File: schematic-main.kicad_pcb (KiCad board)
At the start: 2 copper layers, 100 x 100 mm, 115 parts, among them J1 Fell_Cell_Conn_01x02_Pin, J2 CAN, J3 P_Valve, J5 PWM_Out, J7 Axilary_Out, J8 Temp, J9 Analog_In, P1 USB_C_Plug_USB2.0, U1 LM76202-Q1, U2 TPS62933, U3 USBLC6-2P6, U4 ESP32-S3FN8, U5 SN65HVD232, U6 LM5013DDAR, U7 PC817, U8 PC817, U9 PC817

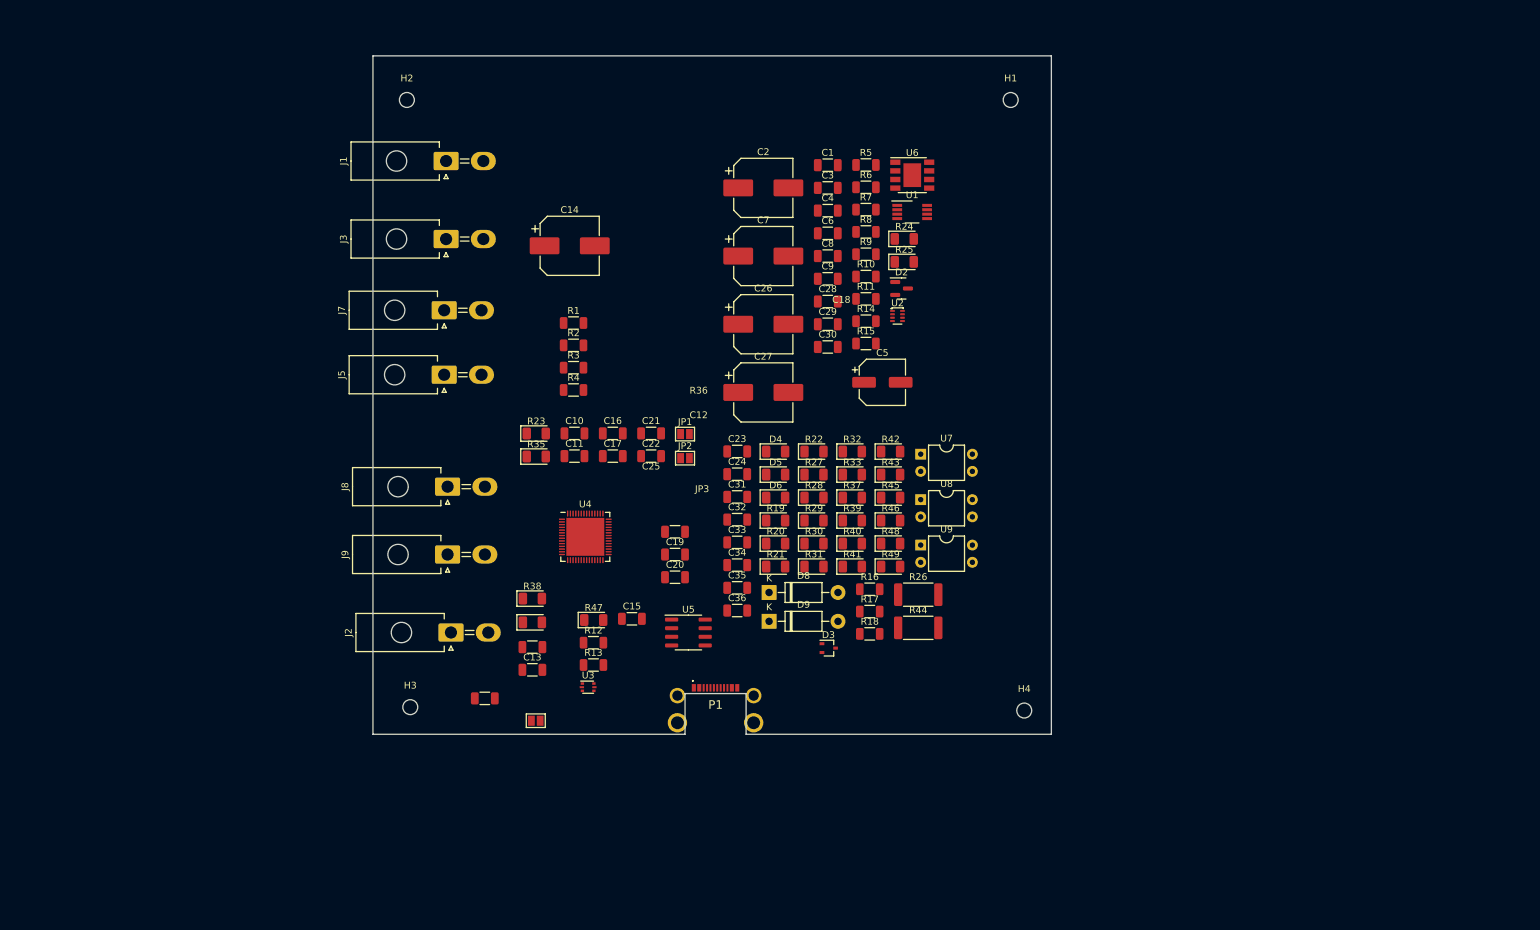
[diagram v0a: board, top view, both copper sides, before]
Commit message: Change FC connector to 10pin & ideal diode sircuit
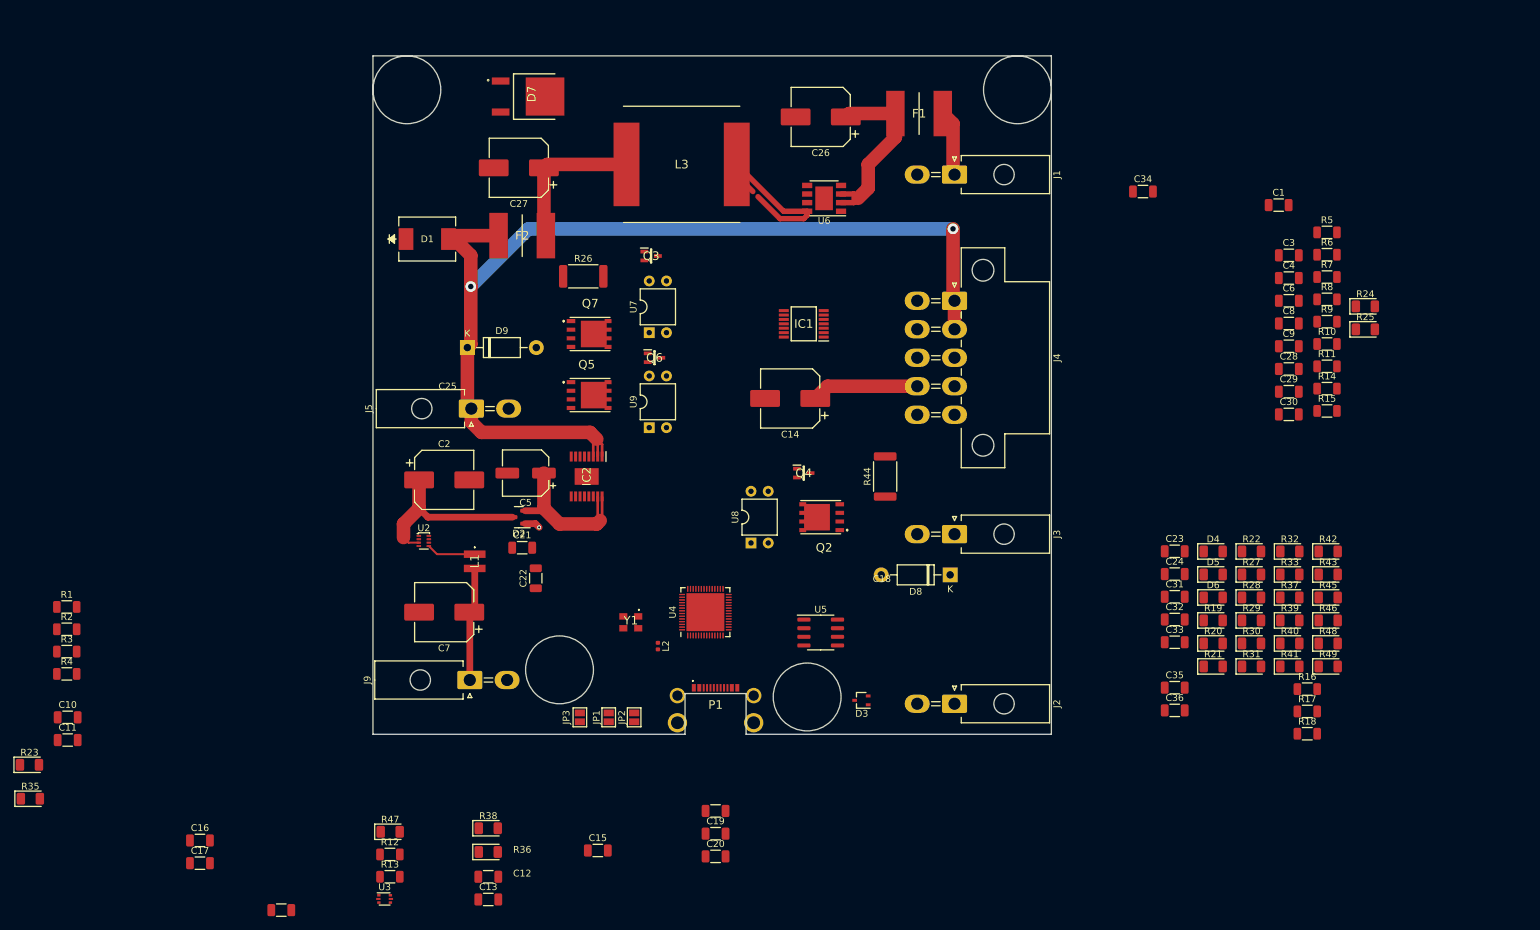
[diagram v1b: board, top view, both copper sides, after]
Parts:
- removed H1, H2, H3, H4: MountingHole, MountingHole:MountingHole_2.2mm_M2
- removed J7: Axilary_Out, Connector_Molex:Molex_Mini-Fit_Jr_5569-02A2_2x01_P4.20mm_Horizontal
- removed J8: Temp, Connector_Molex:Molex_Mini-Fit_Jr_5569-02A2_2x01_P4.20mm_Horizontal
- removed U1: LM76202-Q1, Package_SO:VSSOP-8_3.0x3.0mm_P0.65mm
- added D1: TPSMC30CA, lib:TPSMCSeries_LTF, F.Cu at (98.5, 42.5)
- added D7: MBRD20100CT-13, MBRD20100CT-13:TO252_(DPAK)_1, F.Cu at (109.3, 21.5)
- added F1: 3A, mbr:FUSC8664X180N, F.Cu at (171.0, 24.0)
- added F2: 3A, mbr:FUSC8664X180N, F.Cu at (112.5, 42.0)
- added IC1: AD8544ARUZ-REEL, library:SOP65P640X120-14N, F.Cu at (154.0, 55.0)
- added IC2: LM76202QPWPRQ1, mbr:SOP65P640X120-17N, F.Cu at (122.0, 77.5)
- added J4: FC Cooling, Connector_Molex:Molex_Mini-Fit_Jr_5569-10A1_2x05_P4.20mm_Horizontal, F.Cu at (176.2, 51.6)
- added L1: 4u7, library:SRN3015TA4R7M, F.Cu at (105.5, 90.0)
- added L2: 2n, Inductor_SMD:L_0402_1005Metric, F.Cu at (132.5, 102.5)
- added L3: IHLP6767DZER470M11, library:IHLP6767DZER470M11, F.Cu at (136.0, 31.5)
- added Q2: sir186, library:SI7141DPT1GE3, F.Cu at (156.5, 83.5)
- added Q3: 2N3904, library:SOT65P220X100-3N, F.Cu at (131.5, 45.0)
- added Q4: 2N3904, library:SOT65P220X100-3N, F.Cu at (154.0, 77.0)
- added Q5: sir186, library:SI7141DPT1GE3, F.Cu at (122.5, 65.5)
- added Q6: 2N3904, library:SOT65P220X100-3N, F.Cu at (132.0, 60.0)
- added Q7: sir186, library:SI7141DPT1GE3, F.Cu at (122.5, 56.5)
- added Y1: Crystal_GND24, library:KC3225K400000C1GE00, F.Cu at (128.5, 99.0)
- J1: value Fell_Cell_Conn_01x02_Pin -> Fell_Cell_IN
- J5: value PWM_Out -> Valve
- P1: footprint Connector_USB:2169900002 -> library:2169900002
- moved R35 90.0 mm to (40.0, 125.0)
- moved R23 89.2 mm to (39.9, 120.0)
- moved J3 86.7 mm to (176.2, 86.0), turned to -90 degrees
- moved C10 85.6 mm to (45.5, 113.0)
- moved C11 85.6 mm to (45.5, 116.3)
- moved R1 85.6 mm to (45.4, 96.7)
- moved R2 85.6 mm to (45.4, 100.0)
- moved R3 85.6 mm to (45.4, 103.3)
- moved R4 85.6 mm to (45.4, 106.6)
- moved C16 85.5 mm to (65.0, 131.2)
- moved C17 85.5 mm to (65.0, 134.5)
- moved C34 81.3 mm to (204.0, 35.5)
- moved U2 77.3 mm to (98.0, 87.0)
- moved J1 75.0 mm to (176.2, 33.0), turned to -90 degrees
- moved J2 75.0 mm to (176.2, 111.0), turned to -90 degrees
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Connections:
- net /IO/PWM_Out renamed /IO/Main_Valve
- net /IO/PWM_Output_MCU renamed /IO/Main_Valve_MCU
- net /MCU/PWM_Output_MCU renamed /MCU/Main_Valve_MCU
- net /PWM_Out renamed /Main_Valve
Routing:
- net +12V: track 0.00 -> 154.2 mm, vias 0 -> 2
- net +3.3V: track 0.00 -> 32.6 mm
- net /Power /SC_V: track 0.00 -> 27.8 mm
- net Net-(D7-K): track 0.00 -> 27.6 mm
- net Net-(U2-VIN): track 0.00 -> 26.3 mm
- net /Power /Vreg: track 0.00 -> 25.0 mm
- net Net-(C27-Pad1): track 0.00 -> 22.5 mm
- net /Power /Vin: track 0.00 -> 9.72 mm
- net Net-(U2-SW): track 0.00 -> 7.26 mm
- net /VBUS: track 0.00 -> 2.29 mm, vias 0 -> 1
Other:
- outline, holes or cut-outs redrawn

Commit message: Complate frist version
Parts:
- removed C32: 20n, Capacitor_SMD:C_1206_3216Metric
- removed D9: 1N5819, Diode_THT:D_DO-41_SOD81_P10.16mm_Horizontal
- removed Q7: sir186, library:SI7141DPT1GE3
- added C37: 20n, Capacitor_SMD:C_1206_3216Metric, F.Cu at (120.5, 59.5)
- added D10: 1N5819, Diode_THT:D_DO-41_SOD81_P10.16mm_Horizontal, F.Cu at (102.4, 60.5)
- added J7: Axilary_Out, Connector_Molex:Molex_Mini-Fit_Jr_5569-02A2_2x01_P4.20mm_Horizontal, F.Cu at (105.0, 53.0)
- added Q1: SIR186LDP-T1-RE3, Lib:SI7141DPT1GE3, F.Cu at (163.0, 83.5)
- Q2, Q5: value sir186 -> SIR186LDP-T1-RE3; footprint library:SI7141DPT1GE3 -> Lib:SI7141DPT1GE3
- moved R9 141.2 mm to (96.0, 95.5), turned to 180 degrees
- moved R25 140.7 mm to (98.5, 30.0)
- moved R7 140.5 mm to (97.5, 91.5), turned to -90 degrees
- moved R35 136.9 mm to (164.0, 67.0), turned to -90 degrees
- moved R24 132.2 mm to (107.0, 27.0)
- moved C6 130.3 mm to (101.5, 91.5), turned to -90 degrees
- moved C3 124.8 mm to (106.5, 82.5), turned to 90 degrees
- moved C4 122.3 mm to (110.0, 88.5), turned to -90 degrees
- moved C8 116.9 mm to (113.5, 88.5), turned to -90 degrees
- moved R5 115.2 mm to (120.0, 72.0), turned to -90 degrees
- moved R43 113.8 mm to (123.5, 55.5), turned to 180 degrees
- moved R6 113.7 mm to (125.5, 87.0), turned to 90 degrees
- moved R10 113.4 mm to (120.5, 83.0), turned to 180 degrees
- moved R8 113.3 mm to (120.5, 76.0), turned to 180 degrees
- moved R11 112.8 mm to (120.0, 80.5), turned to 180 degrees
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- renumbered JP2 to BOOT, D4 to CAN_STATUS, D6 to POWER_3.3V, JP1 to RESET, D5 to STATUS, JP3 to TEST
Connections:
- C26 pad 1: /Power /SC_V -> /IO/SC_V
- C31 pad 1: /IO/PURGE_VALVE_GND -> /IO/PURGE_VALVE
- C6 pad 2: GND -> Net-(U2-FB)
- D8 pad 2: /IO/PURGE_VALVE_GND -> /IO/PURGE_VALVE
- F1 pad 2: /Power /SC_V -> /IO/SC_V
- J3 pad 2: /PURGE_VALVE -> /IO/PURGE_VALVE
- J4 pad 10: /Temp_sensor -> +3.3V
- J4 pad 2: +12V -> /FAN_PWM
- J4 pad 3: /FAN_PWM -> /IO/FAN_1_TACHO
- J4 pad 4: /FAN_PWM -> /IO/FAN_GND
- J4 pad 5: /FAN_1_TACHO -> /IO/Temp_sensor
- J4 pad 6: /FAN_2_TACHO -> +12V
- J4 pad 7: /FAN_GND -> /FAN_PWM
- J4 pad 8: /FAN_GND -> /IO/FAN_2_TACHO
- J4 pad 9: +3.3V -> /IO/FAN_GND
- J5 pad 2: /Main_Valve -> /IO/Main_Valve
- J9 pad 2: /A_Input -> /IO/A_Input
- Q2 pad 1: Net-(Q2-G) -> GND
- Q2 pad 10: (no net) -> /IO/FAN_GND
- Q2 pad 11: (no net) -> /IO/FAN_GND
- Q2 pad 2: /IO/PURGE_VALVE_GND -> GND
- Q2 pad 4: (no net) -> Net-(Q2-G)
- Q2 pad 5: (no net) -> /IO/FAN_GND
- Q2 pad 6: (no net) -> /IO/FAN_GND
- Q2 pad 7: (no net) -> /IO/FAN_GND
- Q2 pad 8: (no net) -> /IO/FAN_GND
- Q2 pad 9: (no net) -> /IO/FAN_GND
- Q5 pad 1: Net-(Q5-G) -> GND
- Q5 pad 10: (no net) -> /IO/Main_Valve
- Q5 pad 11: (no net) -> /IO/Main_Valve
- Q5 pad 2: /IO/FAN_GND -> GND
- Q5 pad 4: (no net) -> Net-(Q5-G)
- Q5 pad 5: (no net) -> /IO/Main_Valve
- Q5 pad 6: (no net) -> /IO/Main_Valve
- Q5 pad 7: (no net) -> /IO/Main_Valve
- Q5 pad 8: (no net) -> /IO/Main_Valve
- Q5 pad 9: (no net) -> /IO/Main_Valve
- R28 pad 2: Net-(Q2-G) -> Net-(Q1-G)
- R29 pad 1: Net-(Q2-G) -> Net-(Q1-G)
- R31 pad 2: Net-(Q5-G) -> Net-(Q2-G)
- R32 pad 1: Net-(Q5-G) -> Net-(Q2-G)
- R35 pad 1: /MCU/FAN_1_TACHO -> /IO/FAN_1_TACHO
- R36 pad 1: /MCU/FAN_2_TACHO -> /IO/FAN_2_TACHO
- R42 pad 2: Net-(Q7-G) -> Net-(Q5-G)
- R43 pad 1: Net-(Q7-G) -> Net-(Q5-G)
- R47 pad 1: /MCU/Main_Valve_MCU -> /IO/Main_Valve_MCU
- R7 pad 2: GND -> Net-(U2-FB)
- R9 pad 1: GND -> Net-(U2-FB)
- U4 pad 31: /MCU/FAN_ON_MCU -> /IO/FAN_ON_MCU
- U4 pad 32: /MCU/FAN_1_TACHO -> /IO/FAN_1_TACHO
- U4 pad 33: /MCU/FAN_2_TACHO -> /IO/FAN_2_TACHO
- U4 pad 42: /MCU/Main_Valve_MCU -> /IO/Main_Valve_MCU
- U4 pad 7: /MCU/Temp_MCU -> /IO/Temp_MCU
- U4 pad 8: /MCU/Analog_MCU -> /IO/Analog_MCU
- U4 pad 9: /MCU/FC_Voltage_MCU -> /IO/FC_Voltage_MCU
- U6 pad 2: /Power /SC_V -> /IO/SC_V
- U6 pad 3: /Power /SC_V -> /IO/SC_V
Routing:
- net GND: track 0.00 -> 944.9 mm, vias 0 -> 197
- net +3.3V: track 32.6 -> 246.0 mm, vias 0 -> 9
- net /IO/FC_Voltage_MCU: track 0.00 -> 154.0 mm, vias 0 -> 4
- net /IO/Temp_MCU: track 0.00 -> 141.6 mm, vias 0 -> 2
- net /IO/Analog_MCU: track 0.00 -> 125.8 mm, vias 0 -> 2
- net /IO/A_Input: track 0.00 -> 114.8 mm, vias 0 -> 3
- net +12V: track 154.2 -> 261.1 mm
- net /VBUS: track 2.29 -> 90.0 mm, vias 1 -> 4
- net /Power /FB_12: track 0.00 -> 63.3 mm, vias 0 -> 2
- net /IO/FAN_1_TACHO: track 0.00 -> 61.2 mm, vias 0 -> 2
- net /IO/FAN_2_TACHO: track 0.00 -> 59.0 mm, vias 0 -> 2
- net /IO/Main_Valve_MCU: track 0.00 -> 54.4 mm, vias 0 -> 2
- net Net-(P1-VCONN): track 0.00 -> 50.3 mm, vias 0 -> 2
- net Net-(D7-K): track 27.6 -> 74.8 mm
- net /IO/LED_CAN_STATUS: track 0.00 -> 42.1 mm, vias 0 -> 4
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- added copper zone on B.Cu, net GND
- added copper zone on F.Cu, net GND
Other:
- outline, holes or cut-outs redrawn

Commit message: New pcb 1
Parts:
- removed BOOT, RESET, TEST: SolderJumper_2_Open, Jumper:SolderJumper-2_P1.3mm_Open_Pad1.0x1.5mm
- removed the C1 at (130.5, 73.5)
- removed the C15 at (117.0, 111.5)
- removed the C19 at (140.0, 86.5)
- removed the C20 at (133.0, 96.0)
- removed the C21 at (128.5, 94.0)
- removed the C29 at (142.5, 51.0)
- removed the C3 at (106.5, 82.5)
- removed the C30 at (133.0, 46.5)
- removed CAN_STATUS, POWER_3.3V, STATUS: LED, Diode_SMD:D_1206_3216Metric
- removed F2: 3A, mbr:FUSC8664X180N
- removed the IC2 at (126.0, 77.5)
- removed the J2 at (176.2, 111.0)
- removed the L1 at (105.5, 90.0)
- removed Q4, Q6: 2N3904, library:SOT65P220X100-3N
- removed Q5: SIR186LDP-T1-RE3, Lib:SI7141DPT1GE3
- removed the R16 at (168.5, 100.5)
- removed the R17 at (182.0, 92.0)
- removed the R18 at (164.5, 113.5)
- removed the R19 at (164.5, 107.0)
- removed the R20 at (180.0, 105.5)
- removed the R24 at (107.0, 27.0)
- removed the R33 at (147.5, 80.0)
- removed R47: 10k, LED_SMD:LED_1206_3216Metric
- removed the R5 at (120.0, 72.0)
- removed U7, U8, U9: PC817, Package_DIP:DIP-4_W7.62mm
- added C12: 100n, Capacitor_SMD:C_1206_3216Metric, F.Cu at (220.7, 88.0)
- added C13: 47p, Capacitor_SMD:C_1206_3216Metric, F.Cu at (220.7, 91.4)
- added C14: 100u, Capacitor_SMD:CP_Elec_8x10.5, F.Cu at (211.2, 91.4)
- added C25: 100n, Capacitor_SMD:C_1206_3216Metric, F.Cu at (244.4, 88.0)
- added C26: 100n, Capacitor_SMD:C_1206_3216Metric, F.Cu at (244.4, 91.4)
- added C28: 10n, Capacitor_SMD:C_1206_3216Metric, F.Cu at (227.0, 55.0)
- added C34: 4n7, Capacitor_SMD:C_1206_3216Metric, F.Cu at (252.8, 111.7)
- added C35: 20n, Capacitor_SMD:C_1206_3216Metric, F.Cu at (252.8, 115.0)
- added C36: 20n, Capacitor_SMD:C_1206_3216Metric, F.Cu at (70.0, 73.0)
- added D4: SP0502BAJT, Package_TO_SOT_SMD:SOT-323_SC-70, F.Cu at (243.8, 118.2)
- added D5: LED, Diode_SMD:D_1206_3216Metric, F.Cu at (44.8, 60.2)
- added D6: LED, Diode_SMD:D_1206_3216Metric, F.Cu at (44.8, 63.6)
- added D9: PMEG10020, library:PMEG10020ELR, F.Cu at (67.0, 80.7)
- added IC1: LM76202QPWPRQ1, library:SOP65P640X120-17N, F.Cu at (81.8, 16.6)
- added J3: CAN, library:39303035, F.Cu at (176.7, 103.6)
- added JP1: SolderJumper_2_Open, Jumper:SolderJumper-2_P1.3mm_Open_Pad1.0x1.5mm, F.Cu at (123.5, 112.5)
- added JP2: SolderJumper_2_Open, Jumper:SolderJumper-2_P1.3mm_Open_Pad1.0x1.5mm, F.Cu at (130.0, 112.5)
- added JP3: SolderJumper_2_Open, Jumper:SolderJumper-2_P1.3mm_Open_Pad1.0x1.5mm, F.Cu at (152.5, 112.5)
- added L3: 2n, Inductor_SMD:L_0402_1005Metric, F.Cu at (252.7, 89.7)
- added R12: 453k, LED_SMD:LED_1206_3216Metric, F.Cu at (220.7, 94.7)
- added R13: 49k9, LED_SMD:LED_1206_3216Metric, F.Cu at (220.7, 98.1)
- added R14: 32k, Resistor_SMD:R_1206_3216Metric, F.Cu at (226.3, 87.6)
- added R35: 1k, LED_SMD:LED_1206_3216Metric, F.Cu at (258.5, 111.7)
- added R36: 1k, LED_SMD:LED_1206_3216Metric, F.Cu at (258.5, 115.1)
- added R45: 100R 0,5W, Resistor_SMD:R_2512_6332Metric, F.Cu at (46.3, 86.5)
- added R46: 100R 0,5W, Resistor_SMD:R_2512_6332Metric, F.Cu at (46.0, 96.5)
- added TP1: FC test, Connector_PinSocket_2.54mm:PinSocket_1x01_P2.54mm_Vertical, F.Cu at (76.0, 73.5)
- added TP10: I/O 1, Connector_PinSocket_2.54mm:PinSocket_1x01_P2.54mm_Vertical, F.Cu at (79.5, 42.0)
- added TP11: I/O 2, Connector_PinSocket_2.54mm:PinSocket_1x01_P2.54mm_Vertical, F.Cu at (79.5, 49.0)
- added TP12: I/O 3, Connector_PinSocket_2.54mm:PinSocket_1x01_P2.54mm_Vertical, F.Cu at (79.5, 56.0)
- added TP13: I/O 4, Connector_PinSocket_2.54mm:PinSocket_1x01_P2.54mm_Vertical, F.Cu at (79.5, 63.5)
- added TP2: GND, Connector_PinSocket_2.54mm:PinSocket_1x01_P2.54mm_Vertical, F.Cu at (55.6, 60.9)
- added TP3: GND, Connector_PinSocket_2.54mm:PinSocket_1x01_P2.54mm_Vertical, F.Cu at (55.6, 65.5)
- added TP4: +12V, Connector_PinSocket_2.54mm:PinSocket_1x01_P2.54mm_Vertical, F.Cu at (55.6, 70.0)
- added TP5: +12V, Connector_PinSocket_2.54mm:PinSocket_1x01_P2.54mm_Vertical, F.Cu at (60.2, 60.9)
- added TP6: +5V, Connector_PinSocket_2.54mm:PinSocket_1x01_P2.54mm_Vertical, F.Cu at (60.2, 65.5)
- added TP7: +5V, Connector_PinSocket_2.54mm:PinSocket_1x01_P2.54mm_Vertical, F.Cu at (60.2, 70.0)
- added TP8: +3.3V, Connector_PinSocket_2.54mm:PinSocket_1x01_P2.54mm_Vertical, F.Cu at (64.8, 60.9)
- added TP9: +3.3V, Connector_PinSocket_2.54mm:PinSocket_1x01_P2.54mm_Vertical, F.Cu at (64.8, 65.5)
- C10: value 100n -> 33n
- C16, C17: value 100n -> 12p
- C18: value 1u -> 100n
- C2: value 10u -> 1u; footprint Capacitor_SMD:CP_Elec_8x10.5 -> Capacitor_SMD:C_1206_3216Metric
- C22: value 12p -> 1u
- C24: value 4n7 -> 100n
- C27: value 22u -> 1u; footprint Capacitor_SMD:CP_Elec_8x10.5 -> Capacitor_SMD:C_1206_3216Metric
- C31: value 20n -> 100n
- C4: value 100n -> 47u; footprint Capacitor_SMD:C_1206_3216Metric -> Capacitor_SMD:CP_Elec_6.3x7.7
- C5: value 47u -> 47p; footprint Capacitor_SMD:CP_Elec_6.3x7.7 -> Capacitor_SMD:C_1206_3216Metric
- C6: value 47p -> 3n3
- C7: value 100u -> 2n7; footprint Capacitor_SMD:CP_Elec_8x10.5 -> Capacitor_SMD:C_1206_3216Metric
- C8: value 33n -> 22u; footprint Capacitor_SMD:C_1206_3216Metric -> Capacitor_SMD:CP_Elec_8x10.5
- C9: value 2n7 -> 10u; footprint Capacitor_SMD:C_1206_3216Metric -> Capacitor_SMD:CP_Elec_8x10.5
- D10, D8: value 1N5819 -> PMEG10020; footprint Diode_THT:D_DO-41_SOD81_P10.16mm_Horizontal -> library:PMEG10020ELR
- D2: value BAS40-05 -> MBRD20100CT-13; footprint Package_TO_SOT_SMD:SOT-23 -> MBRD20100CT-13:TO252_(DPAK)_1
- D3: value SP0502BAJT -> MBRD20100CT-13; footprint Package_TO_SOT_SMD:SOT-323_SC-70 -> MBRD20100CT-13:TO252_(DPAK)_1
- D7: value MBRD20100CT-13 -> LED; footprint MBRD20100CT-13:TO252_(DPAK)_1 -> Diode_SMD:D_1206_3216Metric
- F1: footprint mbr:FUSC8664X180N -> library:FUSC8664X180N
- L2: value 2n -> 4u7; footprint Inductor_SMD:L_0402_1005Metric -> library:SRN3015TA4R7M
- Q1, Q2: value SIR186LDP-T1-RE3 -> PMPB10XNX; footprint Lib:SI7141DPT1GE3 -> library:PMPB15XPAX
- Q3: value 2N3904 -> PMPB10XNX; footprint library:SOT65P220X100-3N -> library:PMPB15XPAX
- R1: value 0 -> 5k1
- R10: value 56k -> 143k
- R11: value 100k -> 56k
- R15: value 143k -> 10k
- R21, R22, R30, R41: value 1k -> 10k
- R25: value 49k9 -> 1k; footprint LED_SMD:LED_1206_3216Metric -> Resistor_SMD:R_1206_3216Metric
- R26: value 100R 0,5W -> 1k; footprint Resistor_SMD:R_2512_6332Metric -> Resistor_SMD:R_1206_3216Metric
- R27: value 1k -> 100R; footprint LED_SMD:LED_1206_3216Metric -> Resistor_SMD:R_1206_3216Metric
- R28: value 100 -> 100R; footprint LED_SMD:LED_1206_3216Metric -> Resistor_SMD:R_1206_3216Metric
- R3: value 5k1 -> 0
- R31: value 100 -> 60; footprint LED_SMD:LED_1206_3216Metric -> Resistor_SMD:R_1206_3216Metric
- R32: value 10k -> 60
- R38: value 10k -> 180R
- R39: value 100 -> 180R
- R40: value 1k -> 180R
- R42: value 100 -> 10k
- R6: value 100k -> 180k
- R7: value 32k -> 12k
- R8: value 12k -> 100k
- R9: value 10k -> 100k
- moved C27 156.1 mm to (244.4, 94.7), turned to 0 degrees
- moved R22 139.7 mm to (250.1, 80.6), turned to 0 degrees
- moved R21 134.4 mm to (250.1, 77.2), turned to 0 degrees
- moved R9 131.5 mm to (226.3, 77.8), turned to 0 degrees
- moved R7 130.4 mm to (226.3, 71.2), turned to 0 degrees
- moved R30 126.4 mm to (44.8, 73.8), turned to 0 degrees
- moved R37 126.0 mm to (258.5, 118.5)
- moved R3 124.3 mm to (225.2, 115.2), turned to 0 degrees
- moved C22 122.6 mm to (244.4, 78.0), turned to 0 degrees
- moved R26 121.5 mm to (61.5, 77.3)
- moved C2 121.0 mm to (220.7, 67.9)
- moved C6 120.4 mm to (220.7, 74.6), turned to 0 degrees
- moved C7 119.0 mm to (220.7, 78.0), turned to 0 degrees
- moved R4 116.9 mm to (225.2, 118.5), turned to 0 degrees
- moved R27 114.5 mm to (61.5, 80.5)
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- renumbered C26 to C1, C12 to C15, C13 to C19, C25 to C20, C14 to C21, C36 to C29, C28 to C3, C35 to C30, C33 to C32, C34 to C33, IC1 to IC2, J9 to J2, J7 to J4, J3 to J5, J5 to J6, J4 to J7, L3 to L1, R12 to R16, R13 to R17, R23 to R18, R36 to R19, R35 to R20, R48 to R23, R49 to R24, R46 to R33, R45 to R34, R14 to R5, U6 to U1
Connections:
- C1 pad 1: /IO/SC_V -> /Power /SC_V
- C10 pad 1: +3.3V -> Net-(U2-SS)
- C11 pad 1: +3.3V -> Net-(U2-VIN)
- C16 pad 1: +3.3V -> /MCU/XTAL_N
- C17 pad 1: VDD3P3 -> /MCU/XTAL_P
- C2 pad 1: Net-(U2-VIN) -> +12V
- C22 pad 1: /MCU/XTAL_P -> +3.3V
- C24 pad 1: Net-(C24-Pad1) -> VDD3P3
- C27 pad 1: Net-(C27-Pad1) -> +3.3V
- C3 pad 1: Net-(D7-K) -> Net-(D2-K)
- C31 pad 1: /IO/PURGE_VALVE -> +3.3V
- C31 pad 2: Net-(C31-Pad2) -> GND
- C4 pad 1: Net-(U2-BST) -> /Power /Vreg
- C4 pad 2: Net-(U2-SW) -> GND
- C5 pad 1: /Power /Vreg -> GND
- C5 pad 2: GND -> Net-(C5-Pad2)
- C6 pad 1: +3.3V -> Net-(C5-Pad2)
- C6 pad 2: Net-(U2-FB) -> +12V
- C7 pad 1: +3.3V -> Net-(IC1-DVDT)
- C8 pad 1: Net-(U2-SS) -> +12V
- C9 pad 1: Net-(IC2-DVDT) -> Net-(U2-VIN)
- D2 pad 1: /VBUS -> GND
- D2 pad 2: /Power /Vreg -> GND
- D2 pad 3: Net-(U2-VIN) -> Net-(D2-K)
- D3 pad 1: /IO/CANH -> /VBUS
- D3 pad 2: /IO/CANL -> /Power /Vreg
- D3 pad 3: GND -> Net-(U2-VIN)
- D7 pad 1: GND -> Net-(D7-K)
- D7 pad 2: GND -> +3.3V
- F1 pad 2: /IO/SC_V -> /Power /SC_V
- L1 pad 1: Net-(D7-K) -> Net-(D2-K)
- L1 pad 2: Net-(C27-Pad1) -> +12V
- L2 pad 1: +3.3V -> Net-(U2-SW)
- L2 pad 2: VDD3P3 -> +3.3V
- Q1 pad 1: GND -> /IO/PURGE_VALVE
- Q1 pad 2: GND -> Net-(Q1-G)
- Q2 pad 1: GND -> /IO/FAN_GND
- Q2 pad 2: GND -> Net-(Q2-G)
- Q3 pad 1: GND -> /IO/Main_Valve
- Q3 pad 2: Net-(Q3-B) -> Net-(Q3-G)
- Q3 pad 3: Net-(Q3-C) -> GND
- R1 pad 1: Net-(P1-D-) -> Net-(P1-VCONN)
- R1 pad 2: /MCU/USB_D- -> GND
- R10 pad 1: Net-(IC2-ILIM) -> Net-(D2-K)
- R10 pad 2: GND -> Net-(C5-Pad2)
- R15 pad 1: Net-(D7-K) -> Net-(U2-FB)
- R15 pad 2: Net-(C29-Pad2) -> GND
- R2 pad 1: Net-(P1-D+) -> Net-(P1-D-)
- R2 pad 2: /MCU/USB_D+ -> /MCU/USB_D-
- R21 pad 1: Net-(D5-K) -> /MCU/FAN_PWM_MCU
- R22 pad 1: Net-(D6-K) -> /IO/Main_Valve_MCU
- R23 pad 2: /IO/SC_V -> /IO/FC_V
- R25 pad 1: GND -> Net-(R25-Pad1)
- R25 pad 2: /Power /FB_12 -> /IO/I/O_1_MCU
- R26 pad 1: Net-(C31-Pad2) -> Net-(R26-Pad1)
- R26 pad 2: GND -> /IO/I/O_2_MCU
- R27 pad 1: +12V -> Net-(R27-Pad1)
- R27 pad 2: Net-(Q3-C) -> /IO/I/O_3_MCU
- R28 pad 1: Net-(Q3-C) -> Net-(R28-Pad1)
- R28 pad 2: Net-(Q1-G) -> /IO/I/O_4_MCU
- R29 pad 1: Net-(Q1-G) -> /IO/I/O_3_MCU
- R3 pad 1: Net-(P1-VCONN) -> Net-(P1-D+)
- R3 pad 2: GND -> /MCU/USB_D+
- R30 pad 1: +12V -> /IO/I/O_4_MCU
- R30 pad 2: Net-(Q4-C) -> GND
- R31 pad 1: Net-(Q4-C) -> Net-(C34-Pad1)
- R31 pad 2: Net-(Q2-G) -> /IO/CANH
- R32 pad 1: Net-(Q2-G) -> Net-(C34-Pad1)
- R32 pad 2: GND -> /IO/CANL
- R37 pad 1: +12V -> Net-(D7-K)
- R37 pad 2: Net-(Q4-B) -> GND
- R38 pad 1: /MCU/FAN_PWM_MCU -> Net-(Q1-G)
- R38 pad 2: GND -> /IO/PURGE_VALVE_MCU
- R39 pad 1: /IO/Main_Valve_MCU -> Net-(Q2-G)
- R39 pad 2: Net-(R39-Pad2) -> /IO/FAN_ON_MCU
- R40 pad 1: +12V -> Net-(Q3-G)
- R40 pad 2: Net-(Q6-B) -> /IO/Main_Valve_MCU
- R41 pad 1: +12V -> Net-(Q1-G)
- R41 pad 2: Net-(Q6-C) -> GND
- R42 pad 1: Net-(Q6-C) -> Net-(Q2-G)
- R42 pad 2: Net-(Q5-G) -> GND
- R43 pad 1: Net-(Q5-G) -> Net-(Q3-G)
- R44 pad 1: Net-(C37-Pad2) -> Net-(C35-Pad2)
- R6 pad 1: /Power /Vreg -> +12V
- R6 pad 2: Net-(IC2-~{FLT}) -> Net-(IC1-OVP)
- R7 pad 1: +3.3V -> Net-(IC1-OVP)
- R7 pad 2: Net-(U2-FB) -> GND
- R9 pad 1: Net-(U2-FB) -> /Power /Vreg
- R9 pad 2: GND -> Net-(IC1-~{FLT})
- U1 pad 2: /IO/SC_V -> /Power /SC_V
- U1 pad 3: /IO/SC_V -> /Power /SC_V
- U1 pad 8: Net-(D7-K) -> Net-(D2-K)
- U2 pad 8: GND -> Net-(U2-FB)
- U4 pad 12: unconnected-(U4-GPIO7/ADC1_CH6-Pad12) -> /MCU/I/O_1_MCU
- U4 pad 13: unconnected-(U4-GPIO8/ADC1_CH7-Pad13) -> /MCU/I/O_2_MCU
- U4 pad 16: unconnected-(U4-GPIO11/ADC2_CH0-Pad16) -> /MCU/I/O_3_MCU
- U4 pad 18: unconnected-(U4-GPIO13/ADC2_CH2-Pad18) -> /MCU/I/O_4_MCU
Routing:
- net GND: track 944.9 -> 68.0 mm, vias 197 -> 16
- net +12V: track 261.1 -> 5.82 mm, vias 2 -> 0
- net +3.3V: track 246.0 -> 14.3 mm, vias 9 -> 1
- net /IO/A_Input: track 114.8 -> 11.8 mm, vias 3 -> 1
- net /IO/Temp_MCU: track 141.6 -> 42.6 mm, vias 2 -> 1
- net /IO/Analog_MCU: track 125.8 -> 34.1 mm, vias 2 -> 1
- net /VBUS: track 90.0 -> 0.00 mm, vias 4 -> 0
- net Net-(D7-K): track 74.8 -> 0.00 mm
- net /IO/FC_Voltage_MCU: track 154.0 -> 92.1 mm, vias 4 -> 1
- net Net-(C27-Pad1): track 59.2 -> 0.00 mm
- net /Power /FB_12: track 63.3 -> 4.16 mm, vias 2 -> 1
- net /IO/FAN_1_TACHO: track 61.2 -> 2.83 mm, vias 2 -> 0
- net /IO/FAN_2_TACHO: track 59.0 -> 0.78 mm, vias 2 -> 0
- net /IO/Main_Valve_MCU: track 54.4 -> 0.00 mm, vias 2 -> 0
- net Net-(P1-VCONN): track 50.3 -> 0.00 mm, vias 2 -> 0
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
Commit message: Power stage pcb complate
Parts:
- moved C28 144.5 mm to (84.2, 32.7)
- moved R11 143.8 mm to (94.0, 28.0), turned to 180 degrees
- moved R8 141.1 mm to (94.0, 25.5), turned to 180 degrees
- moved R9 137.9 mm to (96.0, 32.5), turned to 90 degrees
- moved C7 135.1 mm to (93.5, 32.5), turned to -90 degrees
- moved R7 128.8 mm to (107.0, 22.5), turned to 90 degrees
- moved R6 126.0 mm to (107.0, 27.5), turned to 90 degrees
- moved L2 118.5 mm to (123.6, 47.1), turned to -90 degrees
- moved C2 117.7 mm to (108.3, 33.0), turned to -90 degrees
- moved C4 113.6 mm to (96.5, 38.5), turned to 180 degrees
- moved C11 112.5 mm to (118.4, 37.9), turned to 90 degrees
- moved Q2 109.1 mm to (165.0, 76.0)
- moved D1 108.8 mm to (111.8, 23.2), turned to -90 degrees
- moved Q1 108.1 mm to (163.5, 86.0)
- moved C10 107.9 mm to (122.3, 36.9), turned to 180 degrees
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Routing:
- net GND: track 68.0 -> 371.1 mm, vias 16 -> 35
- net /VBUS: track 0.00 -> 157.4 mm, vias 0 -> 3
- net Net-(U2-VIN): track 0.00 -> 58.9 mm, vias 0 -> 11
- net +3.3V: track 14.3 -> 71.0 mm
- net +12V: track 5.82 -> 61.8 mm
- net /Power /Vreg: track 0.00 -> 32.1 mm, vias 0 -> 12
- net Net-(U2-SW): track 0.00 -> 27.6 mm, vias 0 -> 7
- net Net-(U2-FB): track 0.00 -> 25.2 mm
- net /Power /SC_V: track 0.00 -> 25.1 mm
- net Net-(D2-K): track 20.6 -> 45.1 mm, vias 0 -> 2
- net Net-(IC2-+IN_D): track 20.2 -> 6.78 mm
- net Net-(U2-SS): track 0.00 -> 11.7 mm, vias 0 -> 2
- net (no net): track 10.7 -> 0.00 mm
- net Net-(C5-Pad2): track 0.00 -> 7.99 mm
- net Net-(IC1-DVDT): track 0.00 -> 6.63 mm
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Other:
- outline, holes or cut-outs redrawn
